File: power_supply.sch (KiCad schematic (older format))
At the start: 10 parts, among them P0 CONN_4, U1 MAX660, U3 DMP2066LSD, U9 LM7805

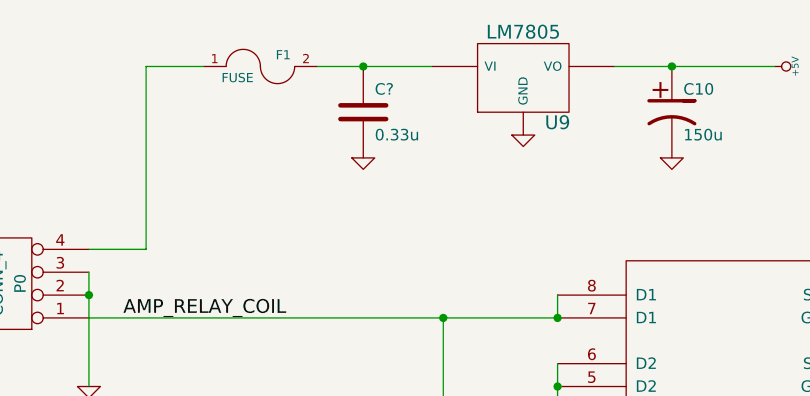
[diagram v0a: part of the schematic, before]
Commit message: Adding part numbers for everything, for BOM preparation.
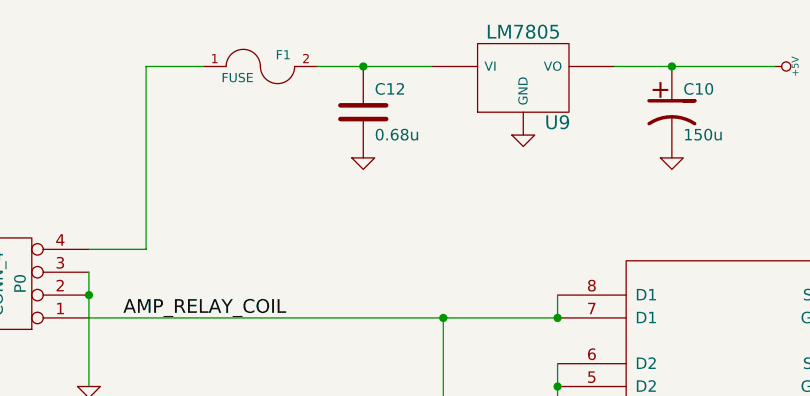
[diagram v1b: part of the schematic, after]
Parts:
- C1, C2: Digikey (none) -> 445-8027-1-ND
- C12: renamed from C?; value 0.33u -> 0.68u; Digikey (none) -> 490-1541-1-ND
- P0: Digikey (none) -> WM4926-ND
- U1: Digikey (none) -> MAX660M-ND
- U3: Digikey (none) -> DMP2066LSDDICT-ND
- U9: DNP (none) -> 1
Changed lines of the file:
@@
-EESchema Schematic File Version 2  date 8/3/2012 1:01:40 PM
+EESchema Schematic File Version 2  date 8/3/2012 4:17:04 PM
 LIBS:atmel
 LIBS:device
@@
 Connection ~ 5450 1900
 $Comp
-L GND #PWR?
+L GND #PWR037
 U 1 1 501C03E7
 P 4100 2300
-F 0 "#PWR?" H 4100 2300 30  0001 C CNN
+F 0 "#PWR037" H 4100 2300 30  0001 C CNN
 F 1 "GND" H 4100 2230 30  0001 C CNN
 	1    4100 2300
@@
 $EndComp
 $Comp
-L C C?
+L C C12
 U 1 1 501C03D0
 P 4100 2100
-F 0 "C?" H 4150 2200 50  0000 L CNN
-F 1 "0.33u" H 4150 2000 50  0000 L CNN
+F 0 "C12" H 4150 2200 50  0000 L CNN
+F 1 "0.68u" H 4150 2000 50  0000 L CNN
+F 4 "490-1541-1-ND" H 4100 2100 60  0001 C CNN "Digikey"
 	1    4100 2100
 	1    0    0    -1
 $EndComp
 $Comp
-L GND #PWR037
+L GND #PWR038
 U 1 1 501C00FA
 P 4800 2200
-F 0 "#PWR037" H 4800 2200 30  0001 C CNN
+F 0 "#PWR038" H 4800 2200 30  0001 C CNN
 F 1 "GND" H 4800 2130 30  0001 C CNN
 	1    4800 2200
@@
 F 1 "LM7805" H 4800 2150 60  0000 C CNN
 F 4 "497-2957-5-ND" H 4800 1950 60  0001 C CNN "Digikey"
+F 5 "1" H 4800 1950 60  0001 C CNN "DNP"
 	1    4800 1950
 	1    0    0    -1
 $EndComp
 $Comp
-L GND #PWR038
+L GND #PWR039
 U 1 1 501BED49
 P 5350 4700
-F 0 "#PWR038" H 5350 4700 30  0001 C CNN
+F 0 "#PWR039" H 5350 4700 30  0001 C CNN
 F 1 "GND" H 5350 4630 30  0001 C CNN
 	1    5350 4700
@@
 $EndComp
 $Comp
-L GND #PWR039
+L GND #PWR040
 U 1 1 501BED47
 P 5450 2300
-F 0 "#PWR039" H 5450 2300 30  0001 C CNN
+F 0 "#PWR040" H 5450 2300 30  0001 C CNN
 F 1 "GND" H 5450 2230 30  0001 C CNN
 	1    5450 2300
@@
 NoConn ~ 2800 4950
 $Comp
-L +5V #PWR040
+L +5V #PWR041
 U 1 1 5019EAE9
 P 3550 4300
-F 0 "#PWR040" H 3550 4390 20  0001 C CNN
+F 0 "#PWR041" H 3550 4390 20  0001 C CNN
 F 1 "+5V" H 3550 4390 30  0000 C CNN
 	1    3550 4300
@@
 $EndComp
 $Comp
-L GND #PWR041
+L GND #PWR042
 U 1 1 5019EADB
 P 3550 5600
-F 0 "#PWR041" H 3550 5600 30  0001 C CNN
+F 0 "#PWR042" H 3550 5600 30  0001 C CNN
 F 1 "GND" H 3550 5530 30  0001 C CNN
 	1    3550 5600
@@
 $EndComp
 $Comp
-L GND #PWR042
+L GND #PWR043
 U 1 1 5019EAD5
 P 4800 5500
-F 0 "#PWR042" H 4800 5500 30  0001 C CNN
+F 0 "#PWR043" H 4800 5500 30  0001 C CNN
 F 1 "GND" H 4800 5430 30  0001 C CNN
 	1    4800 5500
@@
 $EndComp
 $Comp
-L -5V #PWR043
+L -5V #PWR044
 U 1 1 5019EACF
 P 5650 4950
-F 0 "#PWR043" H 5650 5090 20  0001 C CNN
+F 0 "#PWR044" H 5650 5090 20  0001 C CNN
 F 1 "-5V" H 5650 5060 30  0000 C CNN
 	1    5650 4950
@@
 F 0 "C2" H 4850 5400 50  0000 L CNN
 F 1 "15u" H 4850 5200 50  0000 L CNN
+F 4 "445-8027-1-ND" H 4800 5300 60  0001 C CNN "Digikey"
 	1    4800 5300
 	1    0    0    -1
@@
 F 0 "C1" H 4850 4850 50  0000 L CNN
 F 1 "15u" H 4850 4650 50  0000 L CNN
+F 4 "445-8027-1-ND" H 4800 4750 60  0001 C CNN "Digikey"
 	1    4800 4750
 	1    0    0    -1
@@
 F 2 "MODULE" H 3550 4950 50  0001 C CNN
 F 3 "DOCUMENTATION" H 3550 4950 50  0001 C CNN
+F 4 "MAX660M-ND" H 3550 4950 60  0001 C CNN "Digikey"
 	1    3550 4950
 	1    0    0    -1
 $EndComp
 $Comp
-L GND #PWR044
+L GND #PWR045
 U 1 1 50195E98
 P 4950 3450
-F 0 "#PWR044" H 4950 3450 30  0001 C CNN
+F 0 "#PWR045" H 4950 3450 30  0001 C CNN
 F 1 "GND" H 4950 3380 30  0001 C CNN
 	1    4950 3450
@@
 $EndComp
 $Comp
-L +5V #PWR045
+L +5V #PWR046
 U 1 1 50189DC4
 P 6800 2650
-F 0 "#PWR045" H 6800 2740 20  0001 C CNN
+F 0 "#PWR046" H 6800 2740 20  0001 C CNN
 F 1 "+5V" H 6800 2740 30  0000 C CNN
 	1    6800 2650
@@
 $EndComp
 $Comp
-L +5V #PWR046
+L +5V #PWR047
 U 1 1 50189DBE
 P 5900 1900
-F 0 "#PWR046" H 5900 1990 20  0001 C CNN
+F 0 "#PWR047" H 5900 1990 20  0001 C CNN
 F 1 "+5V" H 5900 1990 30  0000 C CNN
 	1    5900 1900
@@
 F 2 "MODULE" H 5400 2700 50  0001 C CNN
 F 3 "DOCUMENTATION" H 5700 2800 50  0001 C CNN
+F 4 "DMP2066LSDDICT-ND" H 5700 3100 60  0001 C CNN "Digikey"
 	1    5700 3100
 	-1   0    0    -1
@@
 AMP_RELAY_COIL
 $Comp
-L GND #PWR047
+L GND #PWR048
 U 1 1 50078FA5
 P 2900 3300
-F 0 "#PWR047" H 2900 3300 30  0001 C CNN
+F 0 "#PWR048" H 2900 3300 30  0001 C CNN
 F 1 "GND" H 2900 3230 30  0001 C CNN
 	1    2900 3300
@@
 F 0 "P0" V 2500 2850 50  0000 C CNN
 F 1 "CONN_4" V 2600 2850 50  0000 C CNN
+F 4 "WM4926-ND" H 2550 2850 60  0001 C CNN "Digikey"
 	1    2550 2850
 	-1   0    0    1
